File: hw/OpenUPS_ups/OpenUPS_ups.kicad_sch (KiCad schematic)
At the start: 5 parts, among them J101 XT60PW-M, U101 AVR32DB28x-xSO

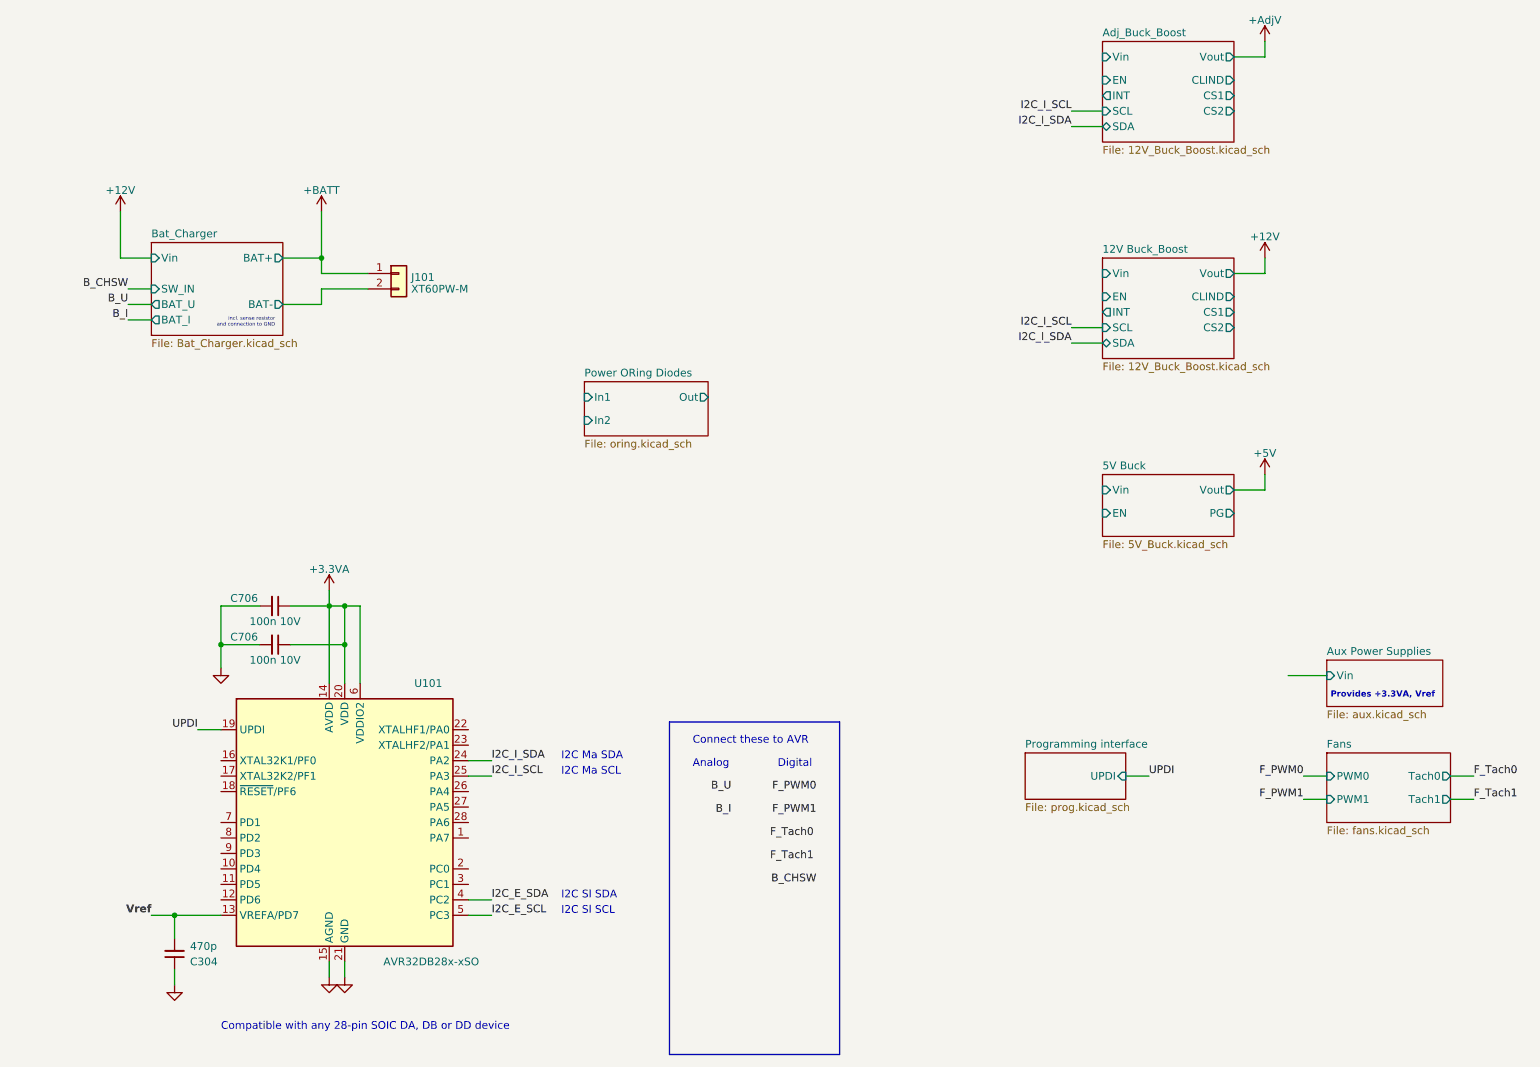
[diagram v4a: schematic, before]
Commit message: Upgraded battery charger with synchronous HB Driver
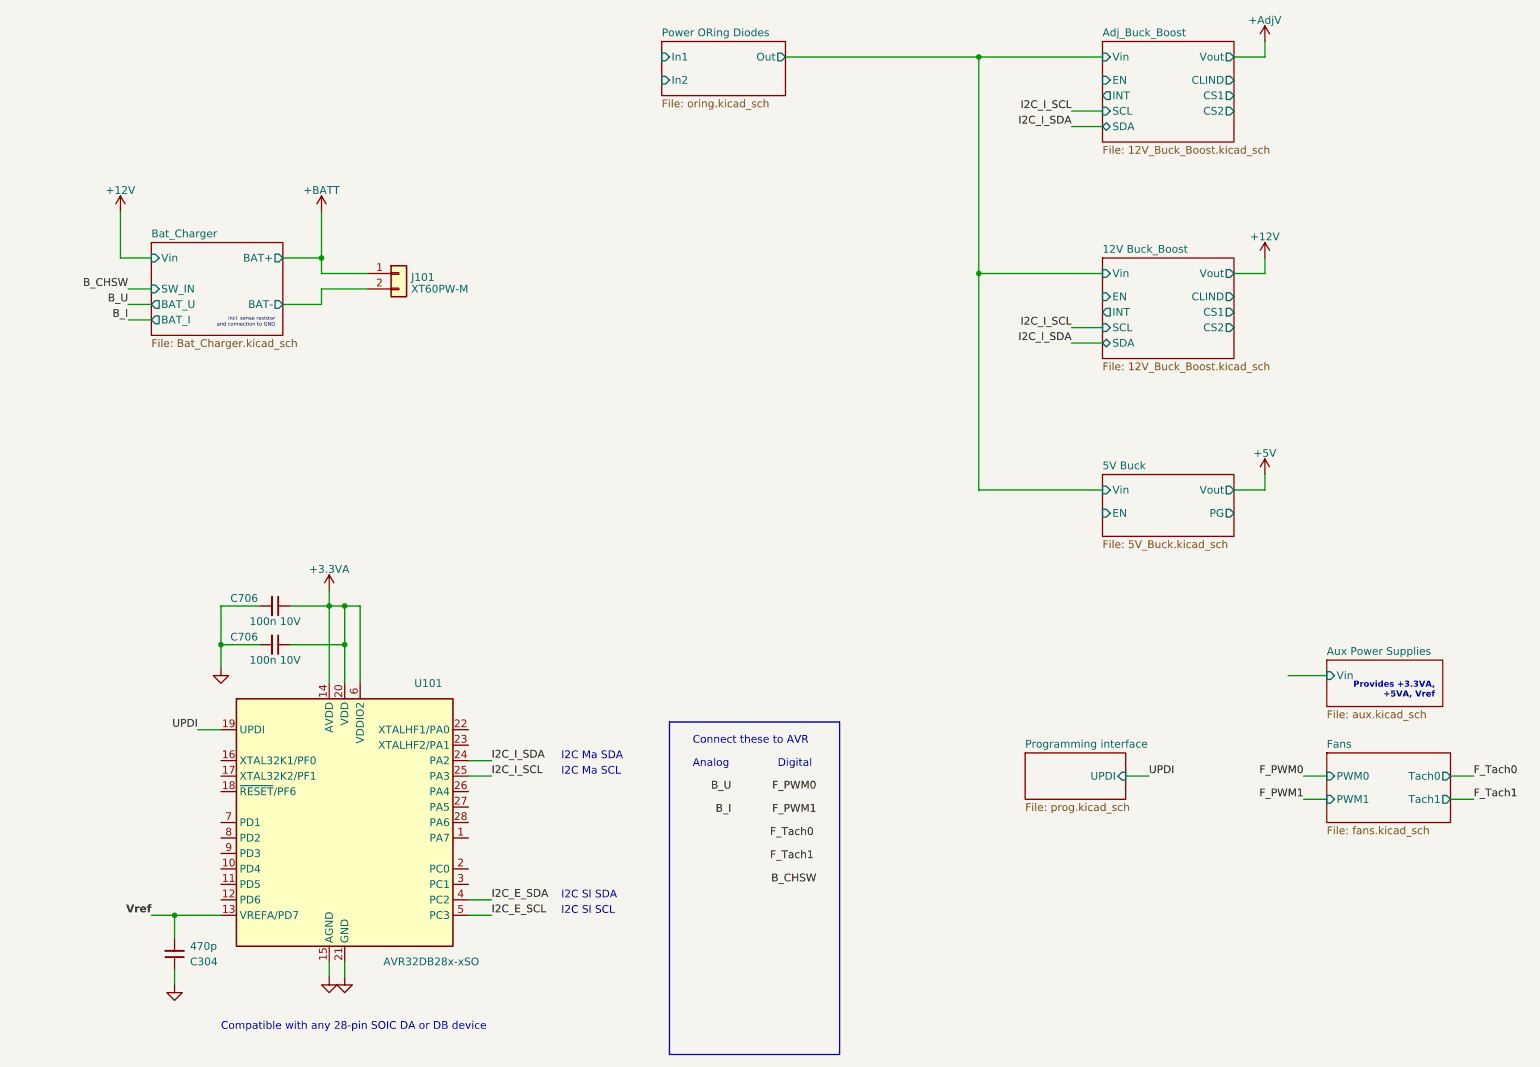
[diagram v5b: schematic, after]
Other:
- note added: "Compatible with any 28-pin SOIC DA or DB device"
- note added: "Provides +3.3VA, +5VA, Vref"
- note removed: "Compatible with any 28-pin SOIC DA, DB or DD device"
- note removed: "Provides +3.3VA, Vref"
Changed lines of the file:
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@@
   (junction (at 63.5 128.27) (diameter 0) (color 0 0 0 0)
   )
+  (junction (at 187.96 31.75) (diameter 0) (color 0 0 0 0)
+  )
+  (junction (at 187.96 67.31) (diameter 0) (color 0 0 0 0)
+  )
   (junction (at 83.82 121.92) (diameter 0) (color 0 0 0 0)
   )
@@
     (stroke (width 0) (type default))
   )
+  (wire (pts (xy 187.96 31.75) (xy 208.28 31.75))
+    (stroke (width 0) (type default))
+  )
   (wire (pts (xy 73.66 72.39) (xy 80.01 72.39))
     (stroke (width 0) (type default))
@@
     (stroke (width 0) (type default))
   )
+  (wire (pts (xy 208.28 102.87) (xy 187.96 102.87))
+    (stroke (width 0) (type default))
+  )
+  (wire (pts (xy 208.28 67.31) (xy 187.96 67.31))
+    (stroke (width 0) (type default))
+  )
   (wire (pts (xy 87.63 67.31) (xy 80.01 67.31))
     (stroke (width 0) (type default))
@@
     (stroke (width 0) (type default))
   )
+  (wire (pts (xy 187.96 102.87) (xy 187.96 67.31))
+    (stroke (width 0) (type default))
+  )
   (wire (pts (xy 203.2 78.74) (xy 208.28 78.74))
     (stroke (width 0) (type default))
@@
     (stroke (width 0) (type default))
   )
+  (wire (pts (xy 156.21 31.75) (xy 187.96 31.75))
+    (stroke (width 0) (type default))
+  )
   (wire (pts (xy 203.2 76.2) (xy 208.28 76.2))
     (stroke (width 0) (type default))
@@
     (stroke (width 0) (type default))
   )
+  (wire (pts (xy 187.96 67.31) (xy 187.96 31.75))
+    (stroke (width 0) (type default))
+  )
   (wire (pts (xy 48.26 74.93) (xy 52.07 74.93))
     (stroke (width 0) (type default))
@@
     (fill (type none))
   )
-  (text "Provides +3.3VA, Vref" (at 262.89 137.16 0)
+  (text "Provides +3.3VA,\n+5VA, Vref" (at 262.89 137.16 0)
     (effects (font (size 1 1) bold) (justify right bottom))
   )
@@
     (effects (font (size 0.6 0.6)) (justify right bottom))
   )
-  (text "Compatible with any 28-pin SOIC DA, DB or DD device"
-    (at 63.5 191.77 0)
+  (text "Compatible with any 28-pin SOIC DA or DB device" (at 63.5 191.77 0)
     (effects (font (size 1.27 1.27)) (justify left bottom))
   )
@@
     )
   )
-  (sheet (at 123.19 85.09) (size 20.32 8.89) (fields_autoplaced)
+  (sheet (at 135.89 29.21) (size 20.32 8.89) (fields_autoplaced)
     (stroke (width 0.1524) (type solid))
     (fill (color 0 0 0 0.0000))
-    (property "Sheetname" "Power ORing Diodes" (at 123.19 84.3784 0)
+    (property "Sheetname" "Power ORing Diodes" (at 135.89 28.4984 0)
       (effects (font (size 1.27 1.27)) (justify left bottom))
     )
-    (property "Sheetfile" "oring.kicad_sch" (at 123.19 94.5646 0)
+    (property "Sheetfile" "oring.kicad_sch" (at 135.89 38.6846 0)
       (effects (font (size 1.27 1.27)) (justify left top))
     )
-    (pin "In1" input (at 123.19 87.63 180)
-      (effects (font (size 1.27 1.27)) (justify left))
-    )
-    (pin "Out" output (at 143.51 87.63 0)
-      (effects (font (size 1.27 1.27)) (justify right))
-    )
-    (pin "In2" input (at 123.19 91.44 180)
-      (effects (font (size 1.27 1.27)) (justify left))
-    )
+    (pin "In1" input (at 135.89 31.75 180)
+      (effects (font (size 1.27 1.27)) (justify left))
+    )
+    (pin "Out" output (at 156.21 31.75 0)
+      (effects (font (size 1.27 1.27)) (justify right))
+    )
+    (pin "In2" input (at 135.89 35.56 180)
+      (effects (font (size 1.27 1.27)) (justify left))
+    )

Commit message: Battery charger HB driver changed to NCP5901
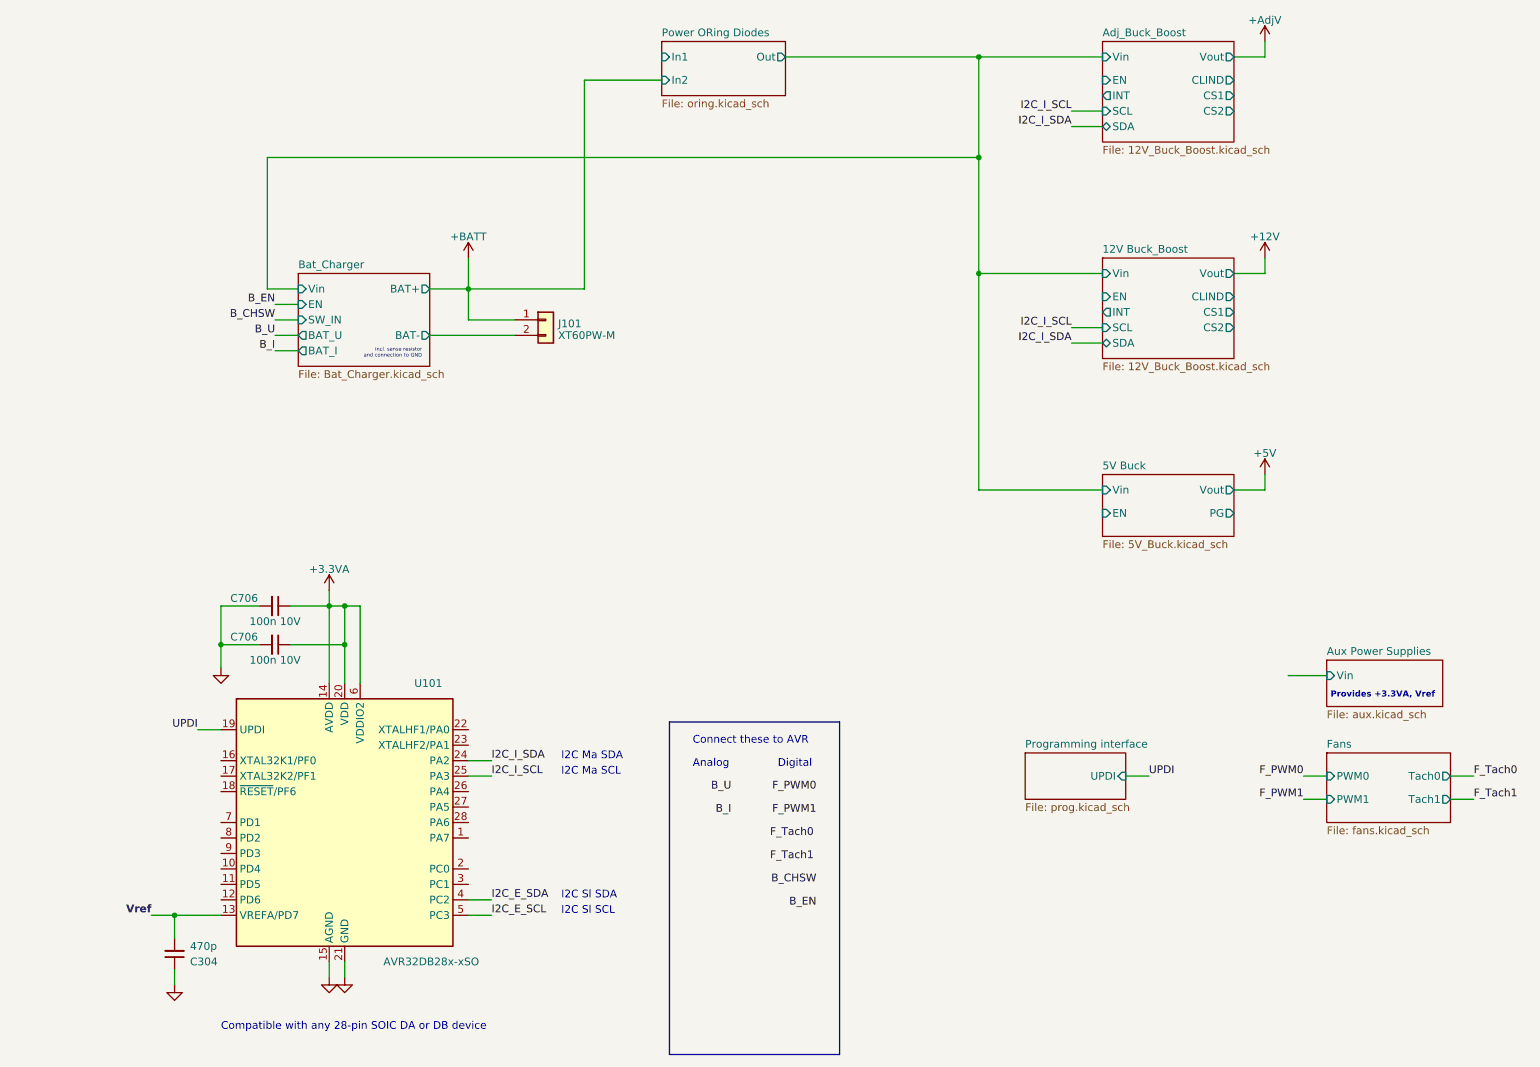
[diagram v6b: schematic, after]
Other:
- sheet Bat_Charger ports: added EN; removed none
- note added: "Provides +3.3VA, Vref"
- note removed: "Provides +3.3VA, +5VA, Vref"
- moved on the sheet: J101

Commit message: 4th generation battery charger
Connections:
- no-connect marks 0 -> 2
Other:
- added sheet Ext. I2C Interface (ext_i2c.kicad_sch)
- sheet Bat_Charger ports: added DAC; removed EN, SW_IN
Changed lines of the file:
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@@
   (junction (at 55.88 172.72) (diameter 0) (color 0 0 0 0)
   )
-  (wire (pts (xy 72.39 72.39) (xy 76.2 72.39))
-    (stroke (width 0) (type default))
-  )
+  (no_connect (at 104.14 165.1))
+  (no_connect (at 104.14 167.64))
   (wire (pts (xy 104.14 74.93) (xy 104.14 69.85))
     (stroke (width 0) (type default))
@@
     (effects (font (size 1.27 1.27)) (justify left bottom))
   )
+  (label "B_DAC" (at 147.32 160.02 180) (fields_autoplaced)
+    (effects (font (size 1.27 1.27)) (justify right bottom))
+  )
   (label "I2C_E_SCL" (at 107.95 172.72 0) (fields_autoplaced)
     (effects (font (size 1.27 1.27)) (justify left bottom))
@@
   (label "I2C_I_SCL" (at 107.95 149.86 0) (fields_autoplaced)
     (effects (font (size 1.27 1.27)) (justify left bottom))
-  )
-  (label "B_EN" (at 72.39 72.39 180) (fields_autoplaced)
-    (effects (font (size 1.27 1.27)) (justify right bottom))
   )
   (label "Vref" (at 52.07 172.72 180) (fields_autoplaced)
@@
     (effects (font (size 1.27 1.27)) (justify left bottom))
   )
-  (label "B_CHSW" (at 72.39 74.93 180) (fields_autoplaced)
+  (label "B_DAC" (at 72.39 74.93 180) (fields_autoplaced)
     (effects (font (size 1.27 1.27)) (justify right bottom))
   )
@@
       (effects (font (size 1.27 1.27)) (justify left))
     )
-    (pin "SW_IN" input (at 76.2 74.93 180)
-      (effects (font (size 1.27 1.27)) (justify left))
-    )
     (pin "Vin" input (at 76.2 69.85 180)
       (effects (font (size 1.27 1.27)) (justify left))
     )
-    (pin "EN" input (at 76.2 72.39 180)
+    (pin "DAC" input (at 76.2 74.93 180)
       (effects (font (size 1.27 1.27)) (justify left))
     )
@@
       )
     )
+  )
+  (sheet (at 144.78 115.57) (size 24.13 12.7) (fields_autoplaced)
+    (stroke (width 0.1524) (type solid))
+    (fill (color 0 0 0 0.0000))
+    (property "Sheetname" "Ext. I2C Interface" (at 144.78 114.8584 0)
+      (effects (font (size 1.27 1.27)) (justify left bottom))
+    )
+    (property "Sheetfile" "ext_i2c.kicad_sch" (at 144.78 128.8546 0)
+      (effects (font (size 1.27 1.27)) (justify left top))
+    )
+    (instances
+      (project "OpenUPS_ups"
+        (path "/f77faec3-eac4-47f3-a2de-ec4a039f4502" (page "10"))
+      )
+    )
